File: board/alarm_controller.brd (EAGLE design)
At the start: 90 x 65 mm, 143 parts, among them IC3 AT24C, X1 RJ45-8L21-S, X2 RJ45-8L21-S

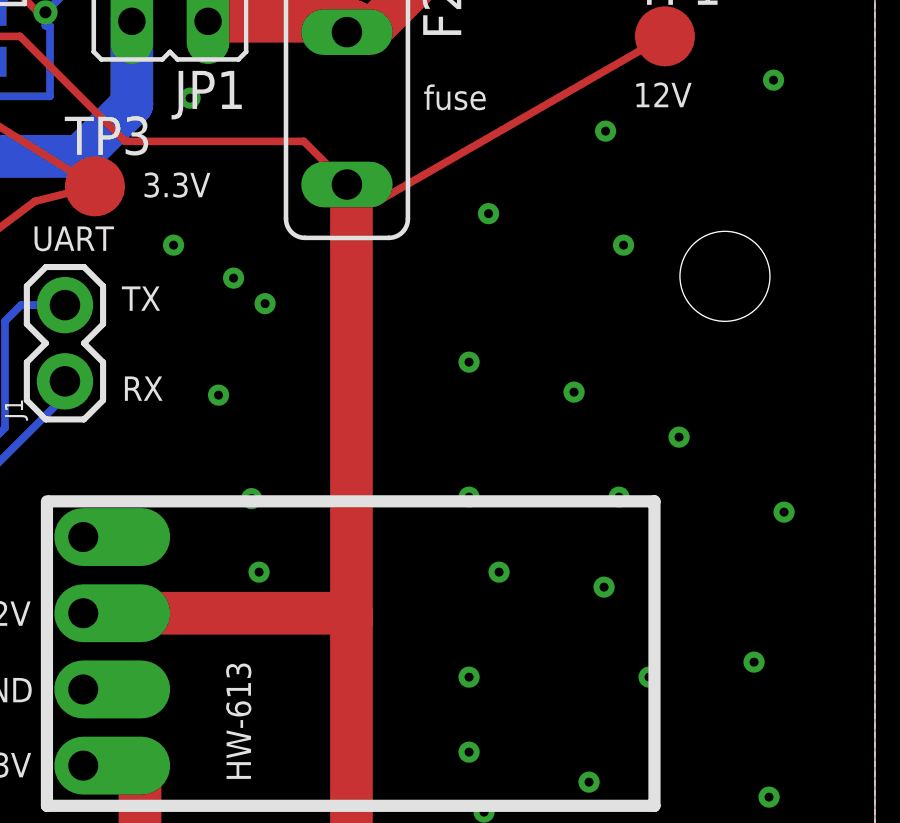
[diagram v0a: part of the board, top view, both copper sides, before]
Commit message: add varistor
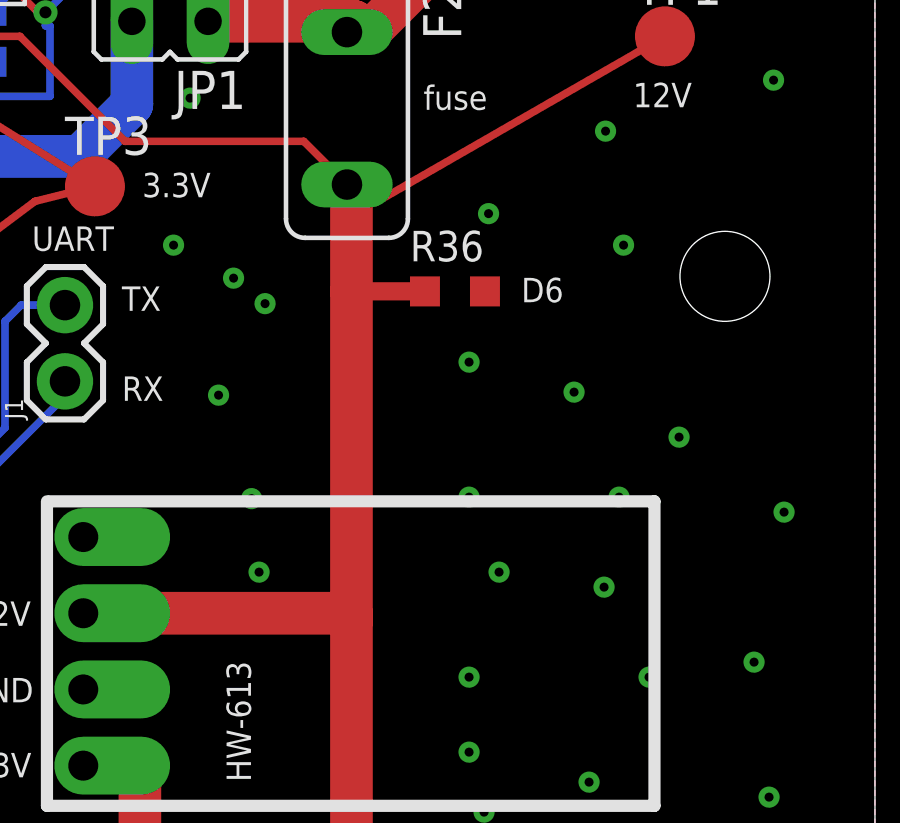
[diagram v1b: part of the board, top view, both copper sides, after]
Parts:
- added R36: VARISTORCN0603, varistor:CT/CN0603
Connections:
- net +12V: now also R36.1
- net GND: now also R36.2
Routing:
- net +12V: track 85.2 -> 87.6 mm
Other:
- board text added: "D6"
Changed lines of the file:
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@@
 PWR</text>
 <text x="55.9" y="38.1" size="0.8128" layer="121">C1</text>
+<text x="78.916" y="44.5428" size="0.8128" layer="121" align="center">D6</text>
 </plain>
 <attributes>
@@
 <element name="J1" library="SparkFun-Connectors" package="1X02" value="" x="63" y="41.5" rot="R90"/>
 <element name="JP1" library="jumper" package="JP1" value="" x="66.5" y="53.5" rot="R90"/>
+<element name="R36" library="varistor" package="CT/CN0603" value="VARISTORCN0603" x="76" y="44.5"/>
 </elements>
 <signals>
@@
 <wire x1="54.22" y1="46.79" x2="54.22" y2="47" width="0.3048" layer="16"/>
 <wire x1="54.22" y1="47" x2="54.3" y2="47" width="0.3048" layer="16"/>
+<contactref element="R36" pad="2"/>
 </signal>
 <signal name="+3V3">
@@
 <wire x1="73" y1="17" x2="73" y2="10" width="1.4224" layer="1"/>
 <wire x1="72.55" y1="47.91" x2="72.55" y2="47.5" width="1.4224" layer="1"/>
-<wire x1="72.55" y1="47.5" x2="72.55" y2="33.5" width="1.4224" layer="1"/>
+<wire x1="72.55" y1="47.5" x2="72.55" y2="44.5" width="1.4224" layer="1"/>
+<wire x1="72.55" y1="44.5" x2="72.55" y2="33.5" width="1.4224" layer="1"/>
 <wire x1="72.55" y1="33.5" x2="72.55" y2="17.75" width="1.4224" layer="1"/>
 <wire x1="72.55" y1="17.75" x2="73" y2="17" width="1.4224" layer="1"/>
@@
 <wire x1="73.36078125" y1="47.46078125" x2="72.58921875" y2="47.46078125" width="0.254" layer="1"/>
 <wire x1="72.58921875" y1="47.46078125" x2="72.55" y2="47.5" width="0.254" layer="1"/>
+<contactref element="R36" pad="1"/>
+<wire x1="75" y1="44.5" x2="72.55" y2="44.5" width="0.6096" layer="1"/>
 </signal>
 <signal name="SWDIO">

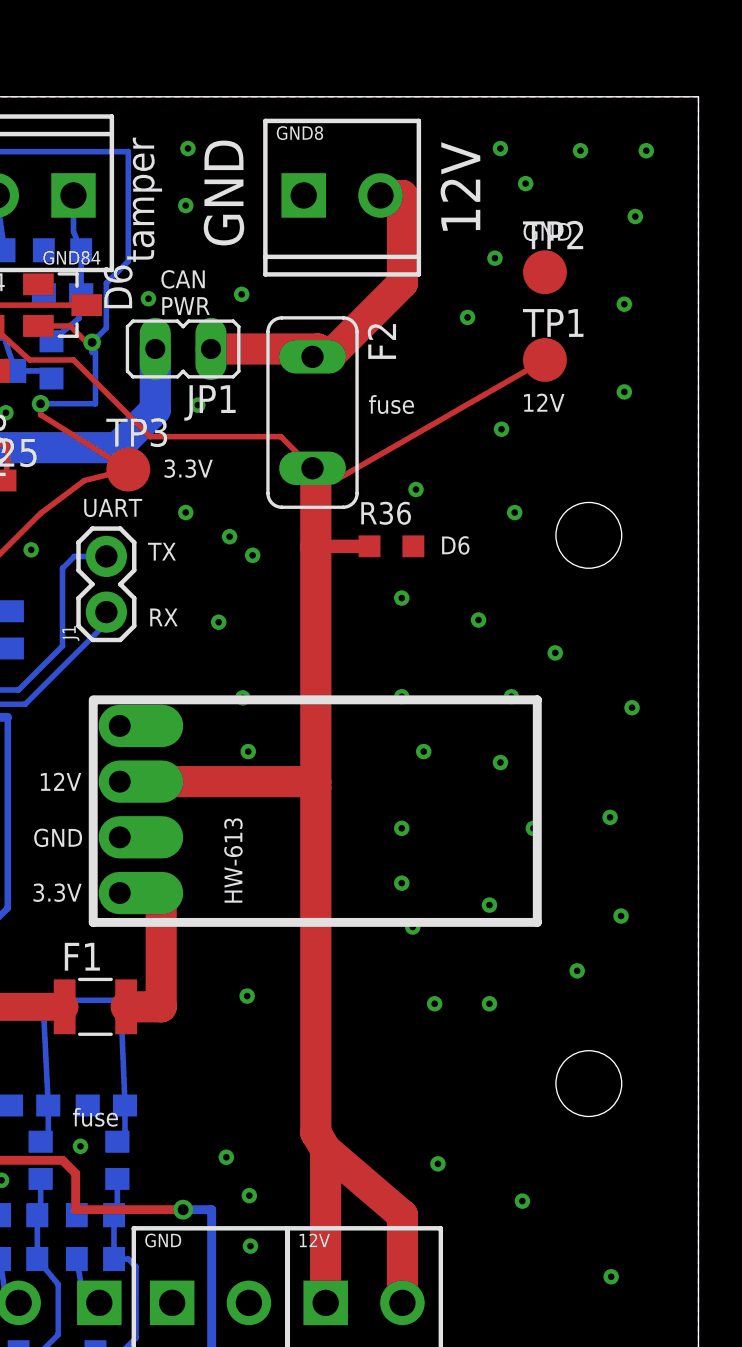
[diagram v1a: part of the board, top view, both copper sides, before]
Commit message: increase 12v and gnd connections
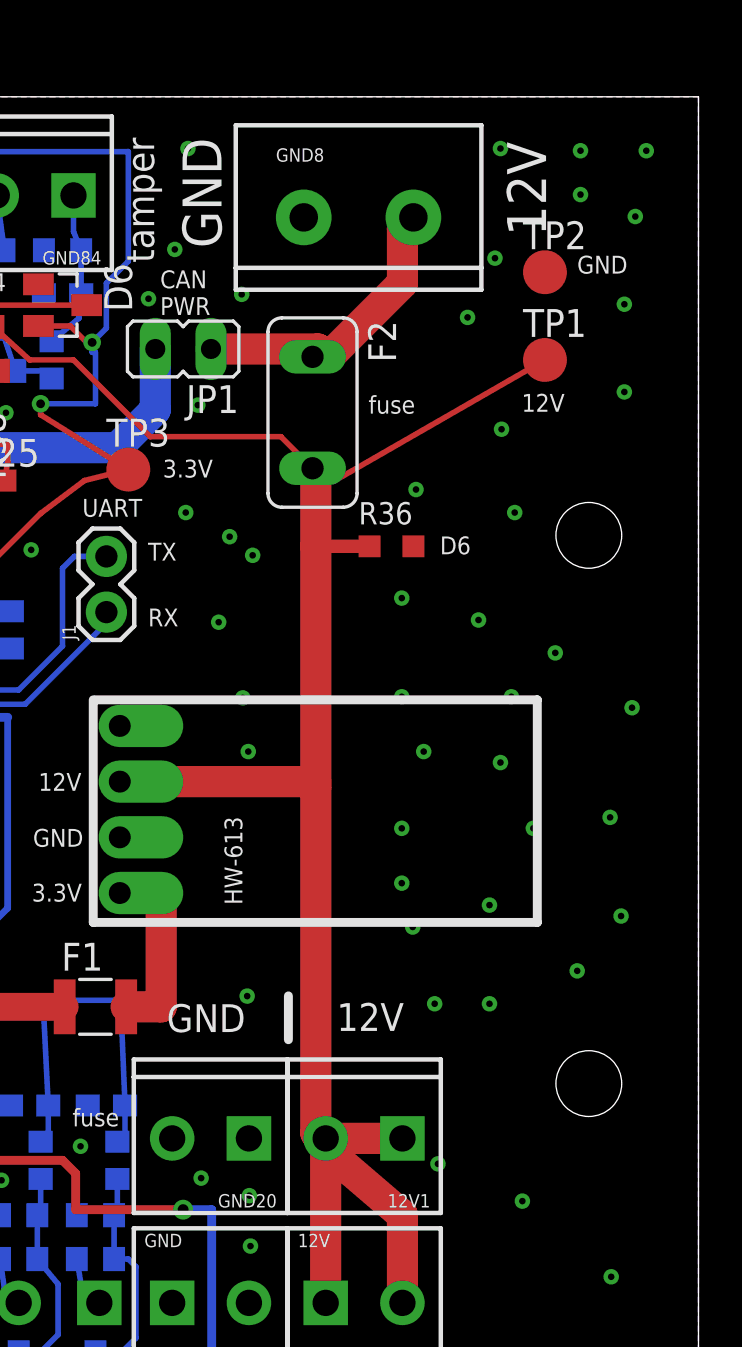
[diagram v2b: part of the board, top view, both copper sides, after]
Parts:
- added 12V1, GND20: (no value), SparkFun-Connectors:SCREWTERMINAL-3.5MM-2
- GND8: device SparkFun-Connectors:SCREWTERMINAL-3.5MM-2 -> SparkFun-Connectors:SCREWTERMINAL-5MM-2
- moved GND8 1.00 mm to (72.0, 59.5)
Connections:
- net +12V: now also 12V1.1, 12V1.2
- net GND: now also GND20.1, GND20.2
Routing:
- net +12V: track 87.6 -> 91.6 mm
- net PRE_FUSE_12V: track 15.9 -> 14.1 mm
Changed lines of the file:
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@@
 <text x="66.716" y="48.0428" size="0.8128" layer="121" align="center">3.3V</text>
 <text x="64.5428" y="60.284" size="1.27" layer="121" rot="R270" align="center">tamper</text>
-<text x="83.116" y="58.8428" size="0.8128" layer="121" align="center">GND</text>
+<text x="85.616" y="57.3428" size="0.8128" layer="121" align="center">GND</text>
 <text x="46.4" y="46.1" size="0.8128" layer="121">R1</text>
 <text x="13" y="3.9" size="1.27" layer="121">1</text>
@@
 <text x="55.87" y="36.8" size="0.6096" layer="122" rot="MR0">sn65hvd</text>
 <circle x="54.92" y="45.09" radius="0.381" width="0.762" layer="121"/>
-<text x="80.05" y="58.65" size="1.778" layer="121" rot="R90">12V</text>
-<text x="69.25" y="58.1" size="1.778" layer="121" rot="R90">GND</text>
+<text x="83.05" y="58.65" size="1.778" layer="121" rot="R90">12V</text>
+<text x="68.25" y="58.1" size="1.778" layer="121" rot="R90">GND</text>
 <wire x1="64.5" y1="5.5" x2="64.5" y2="3.5" width="0.4064" layer="121"/>
 <wire x1="71.3" y1="5.5" x2="71.3" y2="3.5" width="0.4064" layer="121"/>
@@
 <text x="55.9" y="38.1" size="0.8128" layer="121">C1</text>
 <text x="78.916" y="44.5428" size="0.8128" layer="121" align="center">D6</text>
+<wire x1="71.3" y1="24" x2="71.3" y2="22" width="0.4064" layer="121"/>
+<text x="73.5" y="22.4" size="1.27" layer="121">12V</text>
+<text x="65.75" y="22.35" size="1.27" layer="121">GND</text>
 </plain>
 <attributes>
@@
 <attribute name="OC_FARNELL" value="1822206" x="62.5" y="23.5" size="1.778" layer="27" display="off"/>
 </element>
-<element name="GND8" library="SparkFun-Connectors" package="SCREWTERMINAL-3.5MM-2" value="" x="72" y="60.5">
-<attribute name="PROD_ID" value="CONN-08399" x="72" y="60.5" size="1.778" layer="27" display="off"/>
+<element name="GND8" library="SparkFun-Connectors" package="SCREWTERMINAL-5MM-2" value="" x="72" y="59.5">
+<attribute name="SF_SKU" value="PRT-08432" x="72" y="59.5" size="1.778" layer="27" display="off"/>
 </element>
 <element name="F2" library="fuse" package="TE5" value="" x="72.4" y="50.6" rot="R270">
@@
 <element name="JP1" library="jumper" package="JP1" value="" x="66.5" y="53.5" rot="R90"/>
 <element name="R36" library="varistor" package="CT/CN0603" value="VARISTORCN0603" x="76" y="44.5"/>
+<element name="12V1" library="SparkFun-Connectors" package="SCREWTERMINAL-3.5MM-2" value="" x="76.5" y="17.5" rot="R180">
+<attribute name="PROD_ID" value="CONN-08399" x="76.5" y="17.5" size="1.778" layer="27" rot="R180" display="off"/>
+</element>
+<element name="GND20" library="SparkFun-Connectors" package="SCREWTERMINAL-3.5MM-2" value="" x="69.5" y="17.5" rot="R180">
+<attribute name="PROD_ID" value="CONN-08399" x="69.5" y="17.5" size="1.778" layer="27" rot="R180" display="off"/>
+</element>
 </elements>
 <signals>
@@
 <via x="54.47" y="50.64" extent="1-16" drill="0.3" diameter="0.3048"/>
 <via x="56.42" y="56.44" extent="1-16" drill="0.3" diameter="0.3048"/>
-<via x="68.47" y="16.64" extent="1-16" drill="0.3" diameter="0.3048"/>
+<via x="67.32" y="15.69" extent="1-16" drill="0.3" diameter="0.3048"/>
 <via x="61.82" y="17.14" extent="1-16" drill="0.3" diameter="0.3048"/>
 <via x="58.22" y="15.59" extent="1-16" drill="0.3" diameter="0.3048"/>
@@
 <via x="66.72" y="62.64" extent="1-16" drill="0.3" diameter="0.3048"/>
 <via x="80.72" y="57.64" extent="1-16" drill="0.3" diameter="0.3048"/>
-<via x="66.62" y="60.04" extent="1-16" drill="0.3" diameter="0.3048"/>
+<via x="66.12" y="58.04" extent="1-16" drill="0.3" diameter="0.3048"/>
 <via x="36.62" y="46.84" extent="1-16" drill="0.3" diameter="0.3048"/>
 <via x="44.47" y="22.14" extent="1-16" drill="0.3" diameter="0.3048"/>
@@
 <via x="84.62" y="62.54" extent="1-16" drill="0.3" diameter="0.3048"/>
 <via x="87.12" y="59.54" extent="1-16" drill="0.3" diameter="0.3048"/>
-<via x="82.12" y="61.04" extent="1-16" drill="0.3" diameter="0.3048"/>
+<via x="84.62" y="60.54" extent="1-16" drill="0.3" diameter="0.3048"/>
 <via x="86.47" y="27.64" extent="1-16" drill="0.3" diameter="0.3048"/>
 <via x="85.97" y="32.14" extent="1-16" drill="0.3" diameter="0.3048"/>
@@
 <wire x1="54.22" y1="47" x2="54.3" y2="47" width="0.3048" layer="16"/>
 <contactref element="R36" pad="2"/>
+<contactref element="GND20" pad="1"/>
+<contactref element="GND20" pad="2"/>
 </signal>
 <signal name="+3V3">
@@
 <wire x1="72.55" y1="44.5" x2="72.55" y2="33.5" width="1.4224" layer="1"/>
 <wire x1="72.55" y1="33.5" x2="72.55" y2="17.75" width="1.4224" layer="1"/>
-<wire x1="72.55" y1="17.75" x2="73" y2="17" width="1.4224" layer="1"/>
+<wire x1="72.55" y1="17.75" x2="72.911765625" y2="17.147059375" width="1.4224" layer="1"/>
 <contactref element="TP1" pad="TP"/>
+<wire x1="72.911765625" y1="17.147059375" x2="73" y2="17" width="1.4224" layer="1"/>
 <wire x1="83" y1="53" x2="73.36078125" y2="47.46078125" width="0.254" layer="1"/>
 <wire x1="70.96" y1="49.5" x2="65" y2="49.5" width="0.254" layer="1"/>
@@
 <contactref element="R36" pad="1"/>
 <wire x1="75" y1="44.5" x2="72.55" y2="44.5" width="0.6096" layer="1"/>
+<contactref element="12V1" pad="1"/>
+<contactref element="12V1" pad="2"/>
+<wire x1="73" y1="17.5" x2="72.911765625" y2="17.5" width="0.8128" layer="1"/>
+<wire x1="72.911765625" y1="17.5" x2="72.911765625" y2="17.147059375" width="0.8128" layer="1"/>
+<wire x1="76.5" y1="17.5" x2="73" y2="17.5" width="1.4224" layer="1"/>
 </signal>
 <signal name="SWDIO">
@@
 <wire x1="73" y1="53.14" x2="73.14" y2="53.14" width="1.4224" layer="1"/>
 <wire x1="73.14" y1="53.14" x2="76.5" y2="56.5" width="1.4224" layer="1"/>
-<wire x1="76.5" y1="56.5" x2="76.5" y2="60.5" width="1.4224" layer="1"/>
-<wire x1="76.5" y1="60.5" x2="75.5" y2="60.5" width="1.4224" layer="1"/>
+<wire x1="76.5" y1="56.5" x2="76.5" y2="59" width="1.4224" layer="1"/>
+<wire x1="76.5" y1="59" x2="77" y2="59.5" width="1.4224" layer="1"/>
 <contactref element="JP1" pad="1"/>
 <wire x1="67.77" y1="53.5" x2="72.64" y2="53.5" width="1.4224" layer="1"/>

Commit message: refresh eagle libs
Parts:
- removed U$2, U$3: (no value), mounting:DIN-MOUNT-2-HOLE
- added U$5, U$6: (no value), mounting:C45-DIN-MOUNT-2-HOLE
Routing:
- net N$7: track 70.3 -> 71.8 mm
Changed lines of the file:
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@@
 </element>
 <element name="U$4" library="components" package="HW-613" value="HW-613" x="72.5" y="32.5"/>
-<element name="U$2" library="mounting" package="DIN-MOUNT-2-HOLE" value="" x="5" y="32.5"/>
-<element name="U$3" library="mounting" package="DIN-MOUNT-2-HOLE" value="" x="85" y="32.5"/>
 <element name="S1" library="SparkFun-Switches" package="TACTILE_SWITCH_SMD_4.6X2.8MM" value="" x="6" y="12" rot="R90">
 <attribute name="PROD_ID" value="SWCH-13065" x="6" y="12" size="1.778" layer="27" rot="R90" display="off"/>
@@
 <attribute name="PROD_ID" value="CONN-08399" x="69.5" y="17.5" size="1.778" layer="27" rot="R180" display="off"/>
 </element>
+<element name="U$5" library="mounting" package="C45-DIN-MOUNT-2-HOLE" value="" x="5" y="32.5"/>
+<element name="U$6" library="mounting" package="C45-DIN-MOUNT-2-HOLE" value="" x="85" y="32.5"/>
 </elements>
 <signals>
@@
 <via x="3.52" y="13.69" extent="1-16" drill="0.3" diameter="0.3048"/>
 <via x="8.02" y="14.19" extent="1-16" drill="0.3" diameter="0.3048"/>
-<via x="9.47" y="17.94" extent="1-16" drill="0.3" diameter="0.3048"/>
-<via x="9.42" y="20.74" extent="1-16" drill="0.3" diameter="0.3048"/>
+<via x="9.87" y="15.34" extent="1-16" drill="0.3" diameter="0.3048"/>
+<via x="9.77" y="20.79" extent="1-16" drill="0.3" diameter="0.3048"/>
 <via x="13.62" y="20.89" extent="1-16" drill="0.3" diameter="0.3048"/>
 <via x="11.57" y="25.94" extent="1-16" drill="0.3" diameter="0.3048"/>
@@
 <via x="86.62" y="55.54" extent="1-16" drill="0.3" diameter="0.3048"/>
 <via x="86.62" y="51.54" extent="1-16" drill="0.3" diameter="0.3048"/>
-<via x="81.62" y="46.04" extent="1-16" drill="0.3" diameter="0.3048"/>
+<via x="81.12" y="47.54" extent="1-16" drill="0.3" diameter="0.3048"/>
 <via x="78.62" y="2.54" extent="1-16" drill="0.3" diameter="0.3048"/>
 <via x="3.02" y="25.19" extent="1-16" drill="0.3" diameter="0.3048"/>
@@
 <via x="11.5" y="44.5" extent="1-16" drill="0.6"/>
 <wire x1="5.2" y1="9.95" x2="5.2" y2="14.05" width="0.254" layer="1"/>
-<wire x1="5.2" y1="14.05" x2="8" y2="16.85" width="0.254" layer="1"/>
 <wire x1="11.5" y1="28" x2="11.5" y2="44.5" width="0.254" layer="1"/>
-<wire x1="8" y1="16.85" x2="8" y2="24.5" width="0.254" layer="1"/>
-<wire x1="8" y1="24.5" x2="11.5" y2="28" width="0.254" layer="1"/>
+<wire x1="8.5" y1="25" x2="11.5" y2="28" width="0.254" layer="1"/>
+<wire x1="5.2" y1="14.05" x2="5.2" y2="15.7" width="0.254" layer="1"/>
+<wire x1="5.2" y1="15.7" x2="6" y2="16.5" width="0.254" layer="1"/>
+<wire x1="6" y1="16.5" x2="8.5" y2="16.5" width="0.254" layer="1"/>
+<wire x1="8.5" y1="16.5" x2="8.5" y2="25" width="0.254" layer="1"/>
 </signal>
 <signal name="UART_RX">
